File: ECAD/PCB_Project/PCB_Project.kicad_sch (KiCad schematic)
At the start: 0 parts

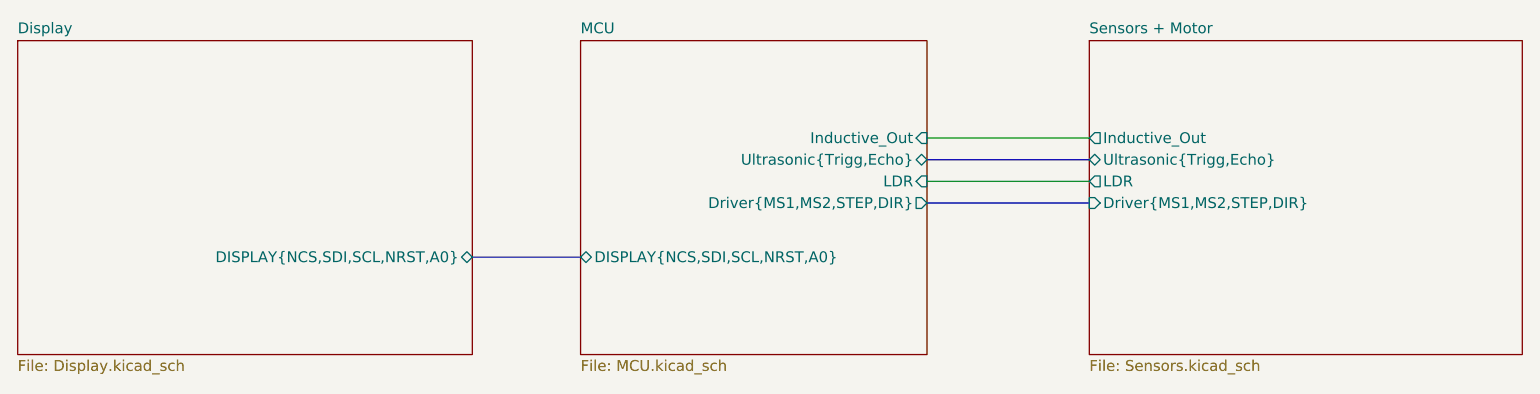
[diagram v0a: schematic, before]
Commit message: Adding Inductive Sensor Transistor
Sims + Schematics
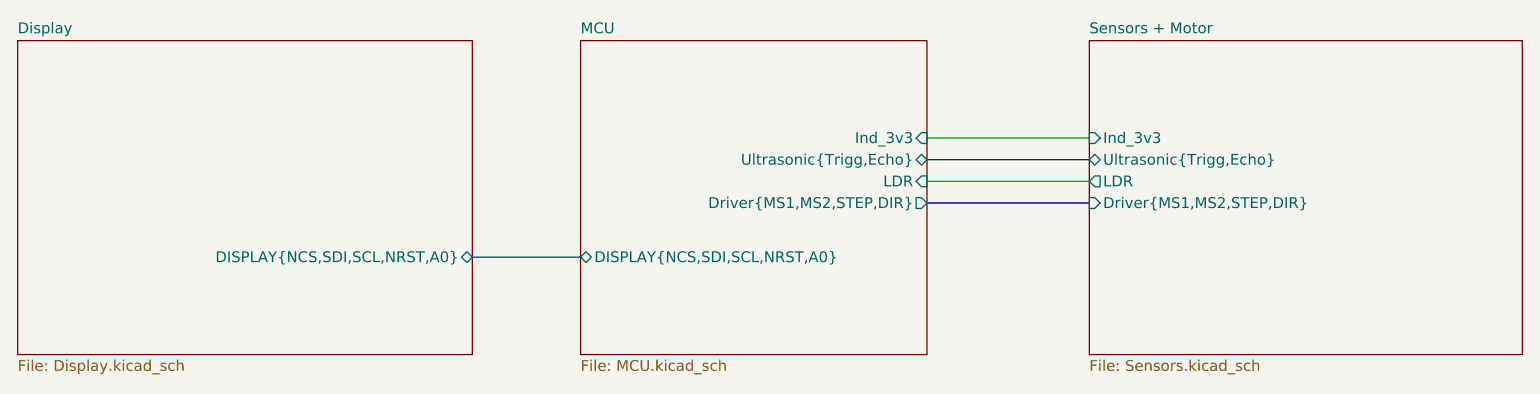
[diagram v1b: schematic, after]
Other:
- sheet MCU ports: added Ind_3v3; removed Inductive_Out
- sheet Sensors + Motor ports: added Ind_3v3; removed Inductive_Out
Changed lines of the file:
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@@
       (effects (font (size 1.27 1.27)) (justify right))
     )
-    (pin "Inductive_Out" input (at 123.19 43.18 0)
+    (pin "Ind_3v3" input (at 123.19 43.18 0)
       (effects (font (size 1.27 1.27)) (justify right))
     )
@@
       (effects (font (size 1.27 1.27)) (justify left top))
     )
-    (pin "Inductive_Out" output (at 142.24 43.18 180)
-      (effects (font (size 1.27 1.27)) (justify left))
-    )
     (pin "Ultrasonic{Trigg,Echo}" bidirectional (at 142.24 45.72 180)
       (effects (font (size 1.27 1.27)) (justify left))
@@
       (effects (font (size 1.27 1.27)) (justify left))
     )
+    (pin "Ind_3v3" input (at 142.24 43.18 180)
+      (effects (font (size 1.27 1.27)) (justify left))
+    )

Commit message: First PCB Draft
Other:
- sheet MCU ports: added SG90_PWM; removed none
- sheet Sensors + Motor ports: added SG90_PWM; removed none
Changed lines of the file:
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@@
+    (stroke (width 0) (type default))
+  )
+  (wire (pts (xy 123.19 40.64) (xy 142.24 40.64))
     (stroke (width 0) (type default))
   )
@@
     )
     (pin "LDR" input (at 123.19 48.26 0)
+      (effects (font (size 1.27 1.27)) (justify right))
+    )
+    (pin "SG90_PWM" output (at 123.19 40.64 0)
       (effects (font (size 1.27 1.27)) (justify right))
     )
@@
       (effects (font (size 1.27 1.27)) (justify left))
     )
-    (pin "Ind_3v3" input (at 142.24 43.18 180)
+    (pin "SG90_PWM" input (at 142.24 40.64 180)
       (effects (font (size 1.27 1.27)) (justify left))
     )
+    (pin "Ind_3v3" output (at 142.24 43.18 180)
+      (effects (font (size 1.27 1.27)) (justify left))
+    )

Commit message: Final PCB
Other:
- sheet MCU ports: added Driver{STEP,DIR}; removed Driver{MS1,MS2,STEP,DIR}
- sheet Sensors + Motor ports: added Driver{STEP,DIR}; removed Driver{MS1,MS2,STEP,DIR}
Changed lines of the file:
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@@
-			)
-		)
-		(pin "Driver{MS1,MS2,STEP,DIR}" output
-			(at 123.19 50.8 0)
-			(effects
-				(font
-					(size 1.27 1.27)
-				)
-				(justify right)
 			)
 		)
@@
 		(pin "Ind_3v3" input
 			(at 123.19 43.18 0)
+			(effects
+				(font
+					(size 1.27 1.27)
+				)
+				(justify right)
+			)
+		)
+		(pin "Driver{STEP,DIR}" output
+			(at 123.19 50.8 0)
 			(effects
 				(font
@@
 			)
 		)
-		(pin "Driver{MS1,MS2,STEP,DIR}" input
-			(at 142.24 50.8 180)
-			(effects
-				(font
-					(size 1.27 1.27)
-				)
-				(justify left)
-			)
-		)
 		(pin "SG90_PWM" input
 			(at 142.24 40.64 180)
@@
 			(effects
 				(font
+					(size 1.27 1.27)
+				)
+				(justify left)
+			)
+		)
+		(pin "Driver{STEP,DIR}" input
+			(at 142.24 50.8 180)
+			(effects
+				(font

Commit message: Pushing
COde changes:
MP driver under development
SG90 as well

PCB:
final version, as sent to manufacture

Sims
New sims for report.
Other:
- company: (none) -> Group 9
- title: (none) -> EE318 - Slam Dunk Your Junk
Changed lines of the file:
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@@
 	(generator_version "8.0")
 	(paper "A5")
+	(title_block
+		(title "EE318 - Slam Dunk Your Junk")
+		(date "2024-05-01")
+		(rev "V1")
+		(company "Group 9")
+		(comment 1 "Manufactured Design")
+	)
 	(bus
 		(pts
